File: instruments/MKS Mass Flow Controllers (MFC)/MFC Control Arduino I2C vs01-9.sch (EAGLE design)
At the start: 60 parts, among them IC1 7812TV, U1 MAX517ACPA+, U2 MAX517ACPA+, U3 MAX517ACPA+, U4 MAX517ACPA+

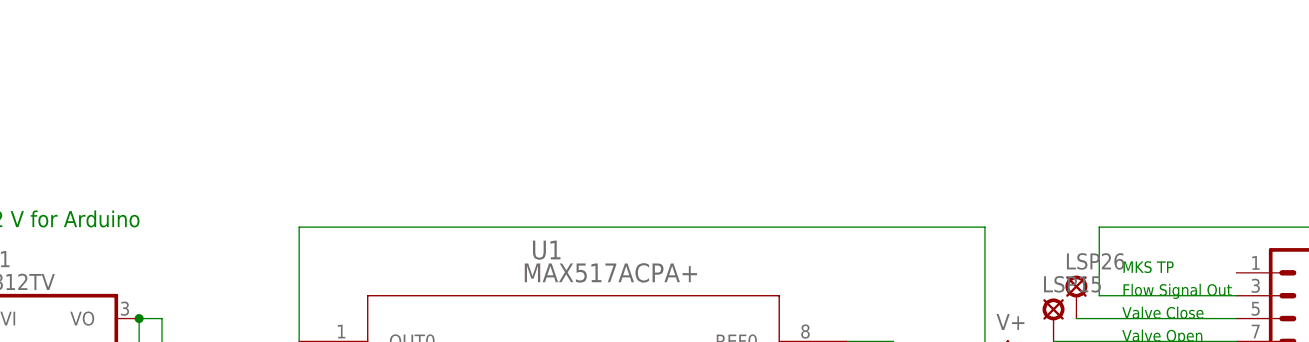
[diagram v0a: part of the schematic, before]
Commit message: many updates, mainly to the LabSmith interface.
System configuration files using LabSmith pumps must be revised
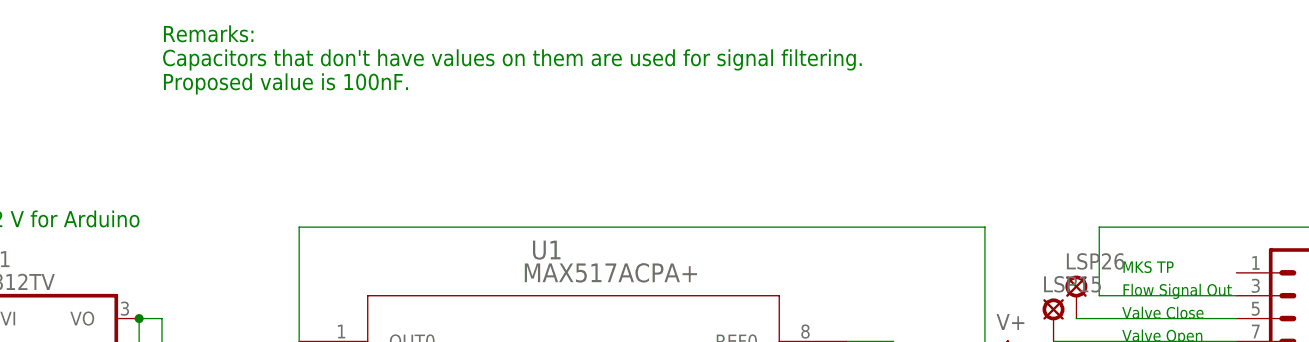
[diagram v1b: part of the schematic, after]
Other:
- note added: "Remarks: Capacitors that don't have values on them are used for signal filtering. Proposed value is 100nF."
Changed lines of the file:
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@@
 <?xml version="1.0" encoding="utf-8"?>
 <!DOCTYPE eagle SYSTEM "eagle.dtd">
-<eagle version="7.2.0">
+<eagle version="6.4">
 <drawing>
 <settings>
@@
 <text x="119.38" y="12.7" size="1.778" layer="91">Flow Signal Output</text>
 <text x="48.26" y="152.4" size="1.778" layer="91">12 V for Arduino</text>
+<text x="68.58" y="167.64" size="1.778" layer="91">Remarks:
+Capacitors that don't have values on them are used for signal filtering.
+Proposed value is 100nF.</text>
 </plain>
 <instances>
@@
 </schematic>
 </drawing>
+<compatibility>
+<note version="6.3" minversion="6.2.2" severity="warning">
+Since Version 6.2.2 text objects can contain more than one line,
+which will not be processed correctly with this version.
+</note>
+</compatibility>
 </eagle>
